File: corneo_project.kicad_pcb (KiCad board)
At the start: 4 copper layers, 54.4 x 74.8 mm, 69 parts, among them J1 Analog input header, J2 GPIO header 1, J4 GPIO header 2, J5 Battery header, J6 USB_C_Receptacle_USB2.0_14P, J7 Debug header, SW1 Keyswitch, SW2 Keyswitch, SW3 Keyswitch, SW4 Keyswitch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

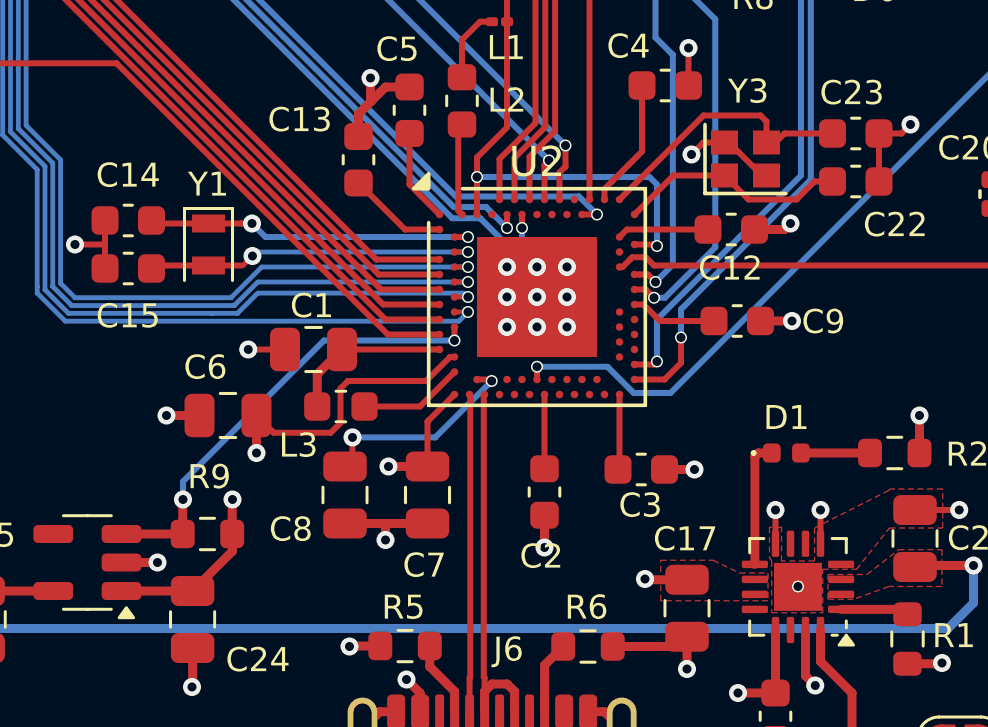
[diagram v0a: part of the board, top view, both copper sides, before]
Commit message: Connectd unconnected pins
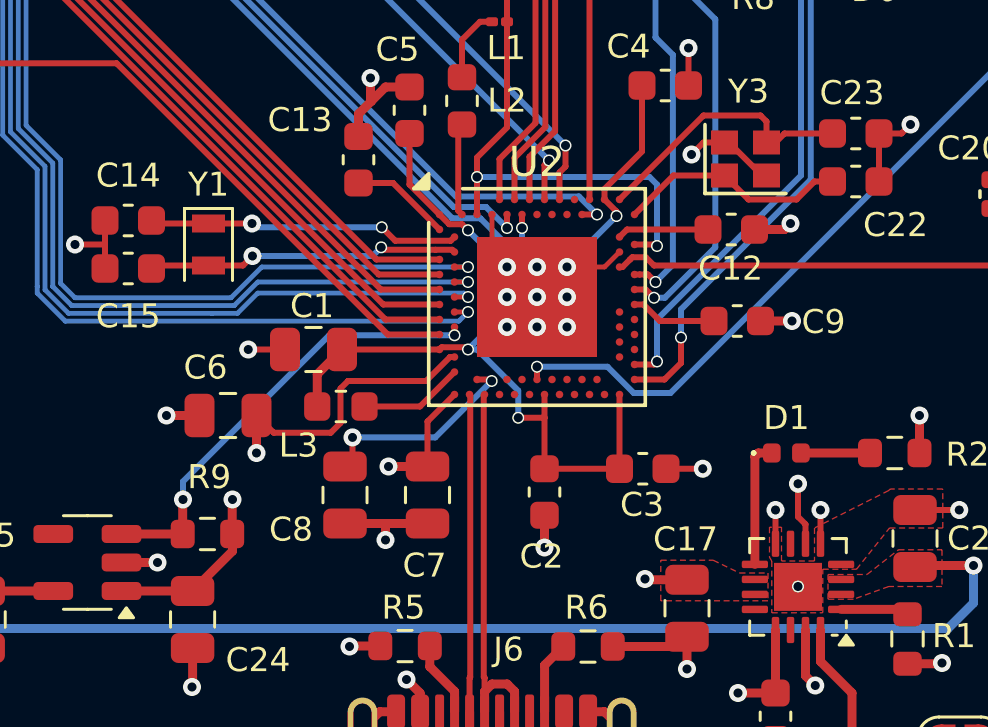
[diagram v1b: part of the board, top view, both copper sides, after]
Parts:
- moved C3 0.06 mm to (89.8, 136.5)
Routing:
- net VDD_NRF: track 17.9 -> 36.6 mm, vias 0 -> 4
- net GND_ANT: track 65.7 -> 69.9 mm
- net VDDH: track 19.5 -> 21.6 mm, vias 5 -> 6
- net Net-(U2-XL1/P0.00): track 11.2 -> 10.4 mm
- net Net-(U2-XL2/P0.01): track 11.2 -> 10.6 mm
